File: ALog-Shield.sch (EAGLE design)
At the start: 26 parts, among them U1 DS3231MZ/V+T

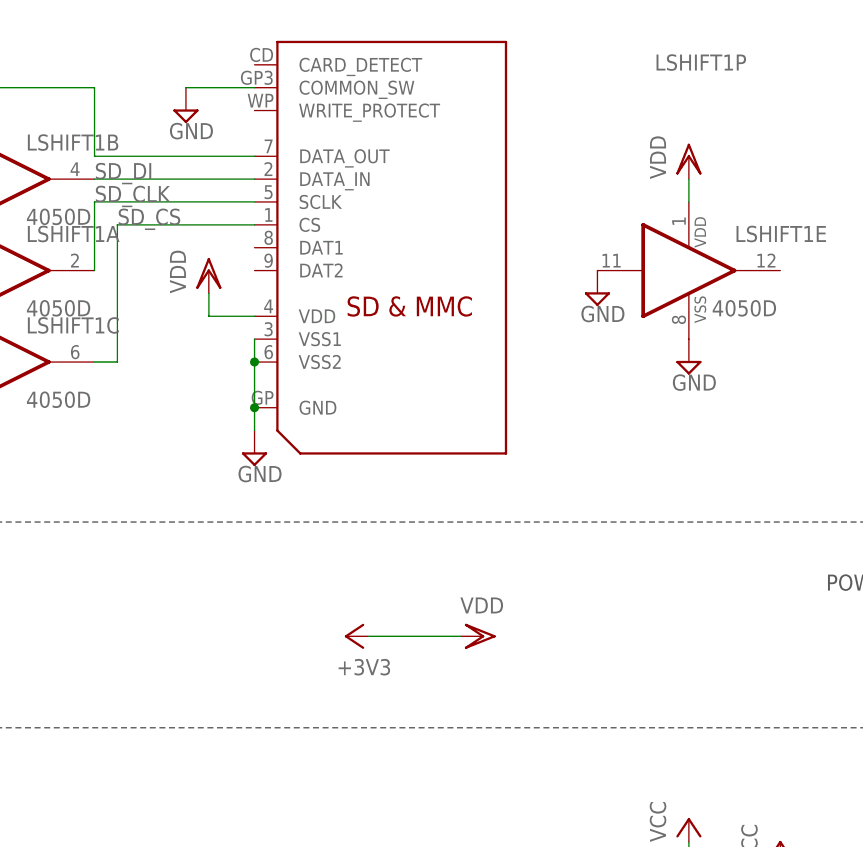
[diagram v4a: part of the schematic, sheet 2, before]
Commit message: 3V3 (not VDD) and VCC
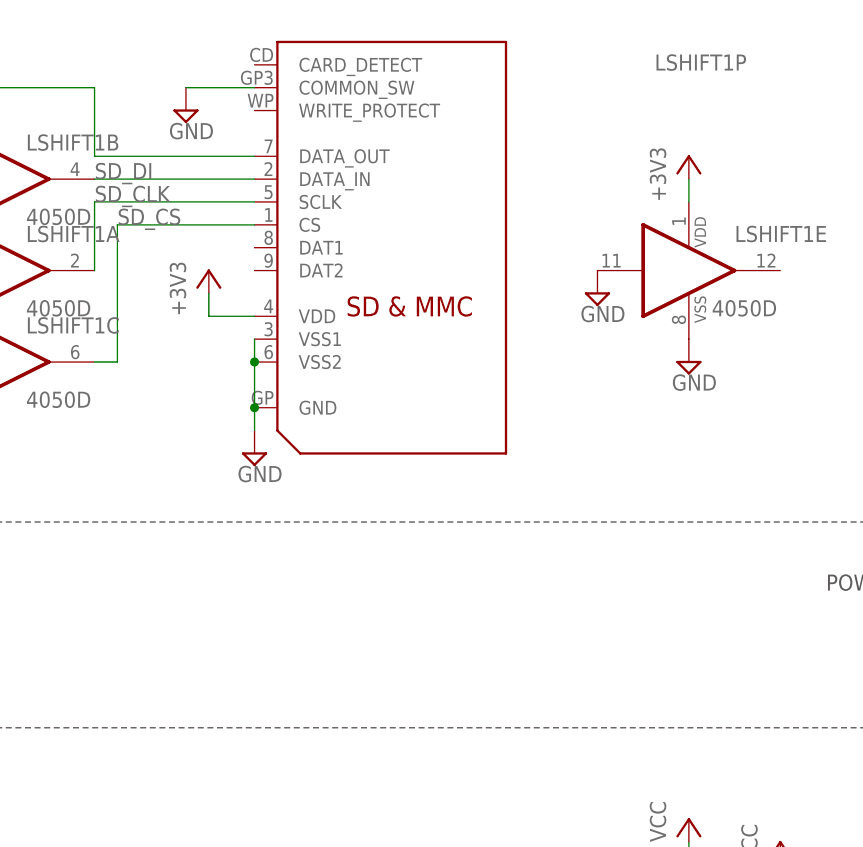
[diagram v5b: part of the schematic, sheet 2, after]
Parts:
- U$9: value ARDUINO_SHIELD_PIN_PURPOSE -> AWICKERT_ARDUINO_SHIELD_PIN_PURPOSE; device awickert:ARDUINO_SHIELD_PIN_PURPOSE -> ALog-Shield:AWICKERT_ARDUINO_SHIELD_PIN_PURPOSE
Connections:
- removed net VDD: LSHIFT1P.VDD, SD1.VDD
- new net VIN: U$9.VIN
- net +3V3: now also LSHIFT1P.VDD, SD1.VDD
- net VCC: now also U$9.5V; no longer U$9.VCC, U$9.VIN
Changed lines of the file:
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@@
 <?xml version="1.0" encoding="utf-8"?>
 <!DOCTYPE eagle SYSTEM "eagle.dtd">
-<eagle version="8.3.1">
+<eagle version="8.5.0">
 <drawing>
 <settings>
-<setting alwaysvectorfont="yes"/>
+<setting alwaysvectorfont="no"/>
 <setting keepoldvectorfont="yes"/>
 <setting verticaltext="up"/>
@@
 <layer number="59" name="tCarbon" color="7" fill="1" visible="no" active="no"/>
 <layer number="60" name="bCarbon" color="7" fill="1" visible="no" active="no"/>
+<layer number="88" name="SimResults" color="9" fill="1" visible="yes" active="yes"/>
+<layer number="89" name="SimProbes" color="9" fill="1" visible="yes" active="yes"/>
 <layer number="90" name="Modules" color="7" fill="1" visible="no" active="yes"/>
 <layer number="91" name="Nets" color="2" fill="1" visible="yes" active="yes"/>
@@
 </classes>
 <parts>
-<part name="U$9" library="awickert" deviceset="ARDUINO_SHIELD_PIN_PURPOSE" device=""/>
+<part name="U$9" library="ALog-Shield" deviceset="AWICKERT_ARDUINO_SHIELD_PIN_PURPOSE" device=""/>
 <part name="+3V3" library="supply1" deviceset="+3V3" device=""/>
 <part name="SUPPLY38" library="supply2" deviceset="GND" device=""/>
 <part name="SUPPLY39" library="supply2" deviceset="GND" device=""/>
 <part name="P+8" library="supply1" deviceset="VCC" device=""/>
-<part name="P+6" library="supply1" deviceset="VCC" device=""/>
 <part name="SUPPLY40" library="supply2" deviceset="GND" device=""/>
 <part name="+3V5" library="supply1" deviceset="+3V3" device=""/>
@@
 <part name="FRAME1" library="frames" deviceset="LETTER_P" device=""/>
 <part name="FRAME3" library="frames" deviceset="LETTER_P" device=""/>
-<part name="+3V15" library="supply1" deviceset="+3V3" device=""/>
-<part name="SD_3V4" library="supply1" deviceset="VDD" device=""/>
-<part name="SD_3V5" library="supply1" deviceset="VDD" device=""/>
-<part name="SD_3V6" library="supply1" deviceset="VDD" device=""/>
 <part name="+3V16" library="supply1" deviceset="+3V3" device=""/>
 <part name="+3V4" library="supply1" deviceset="+3V3" device=""/>
@@
 <part name="LOGO1" library="SparkFun-Aesthetics" deviceset="OSHW-LOGO" device="L"/>
 <part name="J3" library="SparkFun-Connectors" deviceset="M02" device="3.5MM"/>
+<part name="+3V2" library="supply1" deviceset="+3V3" device=""/>
+<part name="+3V7" library="supply1" deviceset="+3V3" device=""/>
 </parts>
 <sheets>
@@
 <instance part="SUPPLY39" gate="GND" x="160.02" y="-60.96"/>
 <instance part="P+8" gate="VCC" x="167.64" y="-53.34"/>
-<instance part="P+6" gate="VCC" x="142.24" y="-45.72"/>
 <instance part="SUPPLY40" gate="GND" x="134.62" y="-71.12"/>
 <instance part="+3V5" gate="G$1" x="152.4" y="-60.96"/>
@@
 <segment>
 <wire x1="124.46" y1="-58.42" x2="154.94" y2="-58.42" width="0.1524" layer="91"/>
-<pinref part="U$9" gate="G$1" pin="VCC"/>
+<pinref part="U$9" gate="G$1" pin="5V"/>
 <label x="129.54" y="-58.42" size="1.778" layer="95"/>
 <wire x1="154.94" y1="-58.42" x2="154.94" y2="-66.04" width="0.1524" layer="91"/>
@@
 <wire x1="154.94" y1="-71.12" x2="154.94" y2="-66.04" width="0.1524" layer="91"/>
 <junction x="154.94" y="-66.04"/>
-</segment>
-<segment>
-<wire x1="124.46" y1="-50.8" x2="142.24" y2="-50.8" width="0.1524" layer="91"/>
-<pinref part="U$9" gate="G$1" pin="VIN"/>
-<wire x1="142.24" y1="-50.8" x2="142.24" y2="-48.26" width="0.1524" layer="91"/>
-<pinref part="P+6" gate="VCC" pin="VCC"/>
 </segment>
 <segment>
@@
 <wire x1="137.16" y1="-139.7" x2="132.08" y2="-139.7" width="0.1524" layer="91"/>
 <label x="132.08" y="-139.7" size="1.778" layer="95"/>
+</segment>
+</net>
+<net name="VIN" class="0">
+<segment>
+<wire x1="124.46" y1="-50.8" x2="134.62" y2="-50.8" width="0.1524" layer="91"/>
+<pinref part="U$9" gate="G$1" pin="VIN"/>
+<label x="129.54" y="-50.8" size="1.778" layer="95"/>
 </segment>
 </net>
@@
 <attribute name="DRAWING_NAME" x="101.6" y="19.05" size="2.54" layer="94"/>
 </instance>
-<instance part="+3V15" gate="G$1" x="76.2" y="175.26" rot="R90"/>
-<instance part="SD_3V4" gate="G$1" x="91.44" y="175.26" rot="R270"/>
-<instance part="SD_3V5" gate="G$1" x="60.96" y="215.9"/>
-<instance part="SD_3V6" gate="G$1" x="114.3" y="228.6"/>
 <instance part="P+5" gate="VCC" x="124.46" y="152.4"/>
 <instance part="P+7" gate="VCC" x="114.3" y="154.94"/>
@@
 </instance>
 <instance part="CLOCK_BATT" gate="G$1" x="137.16" y="121.92" rot="R90"/>
+<instance part="+3V2" gate="G$1" x="60.96" y="215.9"/>
+<instance part="+3V7" gate="G$1" x="114.3" y="228.6"/>
 </instances>
 <busses>
@@
 </segment>
 </net>
-<net name="+3V3" class="0">
-<segment>
-<pinref part="SD_3V4" gate="G$1" pin="VDD"/>
-<pinref part="+3V15" gate="G$1" pin="+3V3"/>
-<wire x1="88.9" y1="175.26" x2="78.74" y2="175.26" width="0.1524" layer="91"/>
-</segment>
-</net>
 <net name="SCL" class="0">
 <segment>
@@
 </segment>
 </net>
-<net name="VDD" class="0">
-<segment>
-<wire x1="60.96" y1="210.82" x2="66.04" y2="210.82" width="0.1524" layer="91"/>
-<pinref part="SD1" gate="G$1" pin="VDD"/>
-<pinref part="SD_3V5" gate="G$1" pin="VDD"/>
-<wire x1="60.96" y1="210.82" x2="60.96" y2="213.36" width="0.1524" layer="91"/>
-</segment>
-<segment>
-<pinref part="LSHIFT1" gate="P" pin="VDD"/>
-<wire x1="114.3" y1="223.52" x2="114.3" y2="226.06" width="0.1524" layer="91"/>
-<pinref part="SD_3V6" gate="G$1" pin="VDD"/>
-</segment>
-</net>
 <net name="CS-SD" class="0">
 <segment>
@@
 </segment>
 </net>
+<net name="+3V3" class="0">
+<segment>
+<pinref part="LSHIFT1" gate="P" pin="VDD"/>
+<wire x1="114.3" y1="223.52" x2="114.3" y2="226.06" width="0.1524" layer="91"/>
+<pinref part="+3V7" gate="G$1" pin="+3V3"/>
+</segment>
+<segment>
+<wire x1="60.96" y1="210.82" x2="66.04" y2="210.82" width="0.1524" layer="91"/>
+<pinref part="SD1" gate="G$1" pin="VDD"/>
+<wire x1="60.96" y1="210.82" x2="60.96" y2="213.36" width="0.1524" layer="91"/>
+<pinref part="+3V2" gate="G$1" pin="+3V3"/>
+</segment>
+</net>

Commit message: Beta for review
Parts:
- added U$1: NWLOGO_MED, awickert:NWLOGO_MED
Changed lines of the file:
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@@
 <?xml version="1.0" encoding="utf-8"?>
 <!DOCTYPE eagle SYSTEM "eagle.dtd">
-<eagle version="8.5.0">
+<eagle version="8.3.1">
 <drawing>
 <settings>
@@
 <part name="+3V2" library="supply1" deviceset="+3V3" device=""/>
 <part name="+3V7" library="supply1" deviceset="+3V3" device=""/>
+<part name="U$1" library="awickert" deviceset="NWLOGO_MED" device=""/>
 </parts>
 <sheets>
@@
 <instance part="LOGO1" gate="G$1" x="17.78" y="-12.7"/>
 <instance part="J3" gate="G$1" x="144.78" y="-137.16" rot="R180"/>
+<instance part="U$1" gate="G$1" x="17.78" y="-27.94"/>
 </instances>
 <busses>

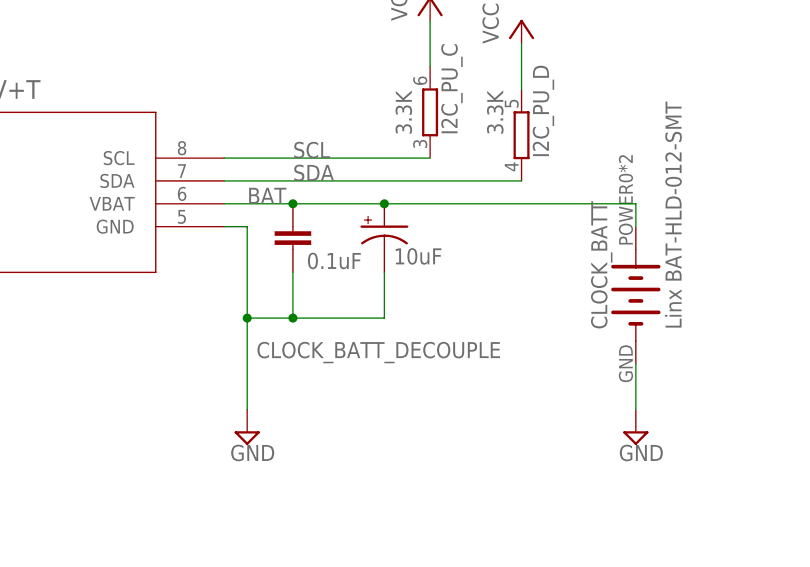
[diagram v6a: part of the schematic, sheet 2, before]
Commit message: 1206-->0805 10uF, rm floating vias
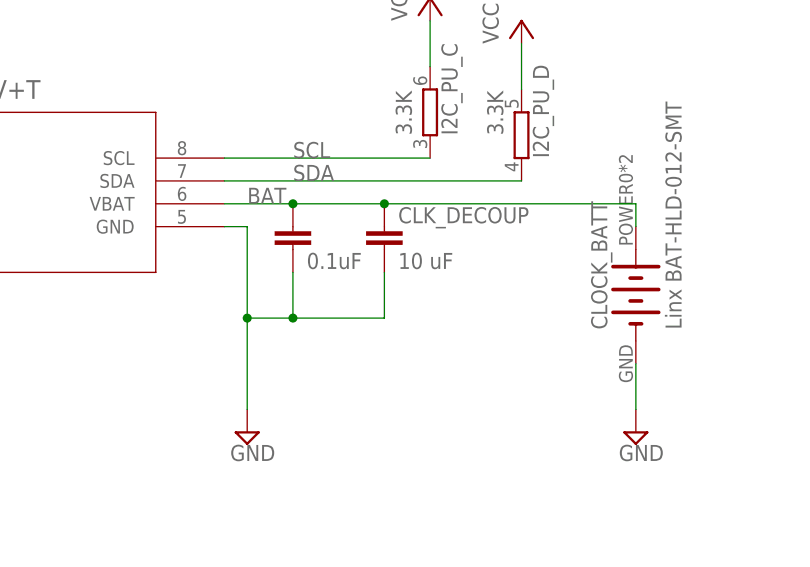
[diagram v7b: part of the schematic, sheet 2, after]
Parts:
- removed CLOCK_BATT_DECOUPLE: 10uF, SparkFun-Passives:CAP_POL1206
- added CLK_DECOUP: 10 uF, SparkFun-Passives:CAP0805
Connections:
- net BAT: now also CLK_DECOUP.1; no longer CLOCK_BATT_DECOUPLE.+
- net GND: now also CLK_DECOUP.2; no longer CLOCK_BATT_DECOUPLE.-
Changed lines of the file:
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@@
 <part name="D2" library="semicon-smd-ipc" deviceset="DIODE_AC-CA_" device="" value="BAT54"/>
 <part name="LOG" library="SparkFun-Electromechanical" deviceset="SWITCH-MOMENTARY-2" device="PTH" value="LOG"/>
-<part name="CLOCK_BATT_DECOUPLE" library="SparkFun-Passives" deviceset="CAP_POL" device="1206" value="10uF"/>
 <part name="U1" library="Maxim-DS3231MZ_8-SOIC" deviceset="DS3231MZ/V+T" device=""/>
 <part name="FRAME1" library="frames" deviceset="LETTER_P" device=""/>
@@
 <part name="+3V7" library="supply1" deviceset="+3V3" device=""/>
 <part name="U$1" library="awickert" deviceset="NWLOGO_MED" device=""/>
+<part name="CLK_DECOUP" library="SparkFun-Passives" deviceset="CAP" device="0805" value="10 uF"/>
 </parts>
 <sheets>
@@
 </segment>
 <segment>
-<wire x1="78.74" y1="-160.02" x2="104.14" y2="-160.02" width="0.1524" layer="91"/>
+<wire x1="58.42" y1="-160.02" x2="104.14" y2="-160.02" width="0.1524" layer="91"/>
 <label x="78.74" y="-160.02" size="1.778" layer="95"/>
 <pinref part="D2" gate="G$1" pin="A2"/>
@@
 </instance>
 <instance part="SUPPLY56" gate="GND" x="137.16" y="106.68"/>
-<instance part="CLOCK_BATT_DECOUPLE" gate="G$1" x="109.22" y="129.54" smashed="yes">
-<attribute name="NAME" x="94.996" y="114.935" size="1.778" layer="95"/>
-<attribute name="VALUE" x="110.236" y="125.349" size="1.778" layer="96"/>
-</instance>
 <instance part="U1" gate="A" x="20.32" y="137.16"/>
 <instance part="FRAME3" gate="G$1" x="0" y="0"/>
@@
 <instance part="+3V2" gate="G$1" x="60.96" y="215.9"/>
 <instance part="+3V7" gate="G$1" x="114.3" y="228.6"/>
+<instance part="CLK_DECOUP" gate="G$1" x="109.22" y="127"/>
 </instances>
 <busses>
@@
 <segment>
 <pinref part="CLOCK_BATT_DECOUP" gate="G$1" pin="2"/>
-<pinref part="CLOCK_BATT_DECOUPLE" gate="G$1" pin="-"/>
 <wire x1="99.06" y1="119.38" x2="99.06" y2="124.46" width="0.1524" layer="91"/>
 <wire x1="109.22" y1="124.46" x2="109.22" y2="119.38" width="0.1524" layer="91"/>
@@
 <junction x="99.06" y="119.38"/>
 <pinref part="U1" gate="A" pin="GND"/>
+<pinref part="CLK_DECOUP" gate="G$1" pin="2"/>
 </segment>
 <segment>
@@
 <label x="93.98" y="132.08" size="1.778" layer="95"/>
 <pinref part="CLOCK_BATT_DECOUP" gate="G$1" pin="1"/>
+<junction x="99.06" y="132.08"/>
 <wire x1="99.06" y1="132.08" x2="109.22" y2="132.08" width="0.1524" layer="91"/>
-<junction x="99.06" y="132.08"/>
-<pinref part="CLOCK_BATT_DECOUPLE" gate="G$1" pin="+"/>
+<pinref part="U1" gate="A" pin="VBAT"/>
 <wire x1="109.22" y1="132.08" x2="137.16" y2="132.08" width="0.1524" layer="91"/>
-<junction x="109.22" y="132.08"/>
-<pinref part="U1" gate="A" pin="VBAT"/>
 <wire x1="137.16" y1="132.08" x2="137.16" y2="129.54" width="0.1524" layer="91"/>
 <pinref part="CLOCK_BATT" gate="G$1" pin="+"/>
-</segment>
-</net>
+<pinref part="CLK_DECOUP" gate="G$1" pin="1"/>
+<junction x="109.22" y="132.08"/>
+</segment>
+</net>

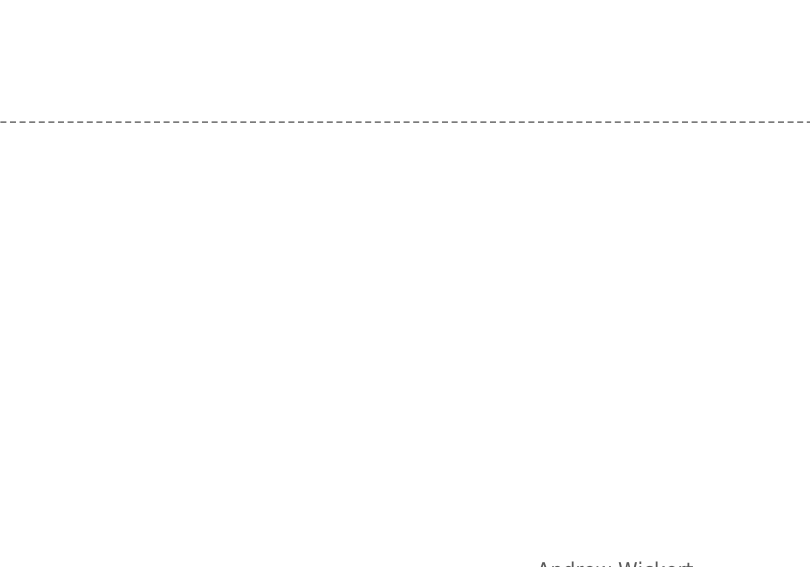
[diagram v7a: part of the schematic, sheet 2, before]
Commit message: AREF to 3V3 jumper
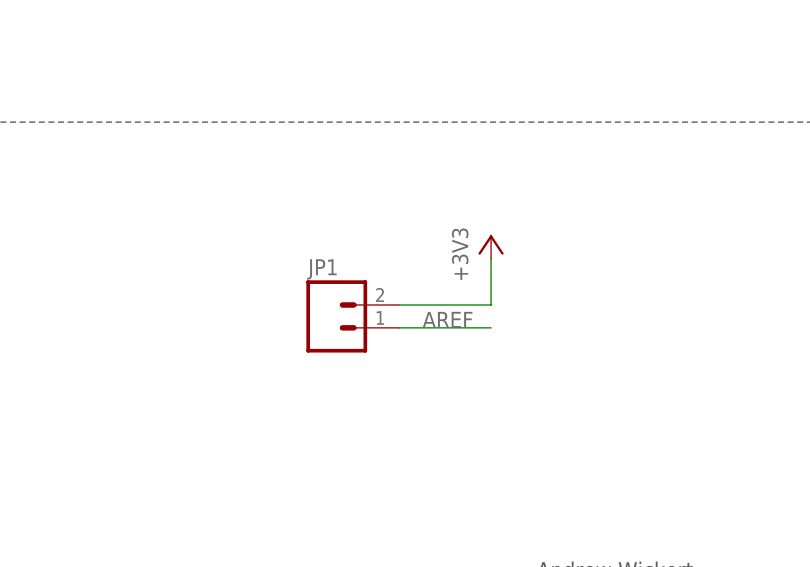
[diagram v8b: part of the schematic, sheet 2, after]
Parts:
- added JP1: (no value), SparkFun-Connectors:M02LOCK
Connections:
- new net AREF: JP1.1, U$9.AREF
- net +3V3: now also JP1.2; no longer U$9.AREF
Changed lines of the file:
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@@
 <parts>
 <part name="U$9" library="ALog-Shield" deviceset="AWICKERT_ARDUINO_SHIELD_PIN_PURPOSE" device=""/>
-<part name="+3V3" library="supply1" deviceset="+3V3" device=""/>
 <part name="SUPPLY38" library="supply2" deviceset="GND" device=""/>
 <part name="SUPPLY39" library="supply2" deviceset="GND" device=""/>
@@
 <part name="U$1" library="awickert" deviceset="NWLOGO_MED" device=""/>
 <part name="CLK_DECOUP" library="SparkFun-Passives" deviceset="CAP" device="0805" value="10 uF"/>
+<part name="JP1" library="SparkFun-Connectors" deviceset="M02" device="LOCK"/>
+<part name="+3V3" library="supply1" deviceset="+3V3" device=""/>
 </parts>
 <sheets>
@@
 <instances>
 <instance part="U$9" gate="G$1" x="91.44" y="-45.72" rot="R90"/>
-<instance part="+3V3" gate="G$1" x="43.18" y="-76.2" rot="R90"/>
 <instance part="SUPPLY38" gate="GND" x="35.56" y="-76.2"/>
 <instance part="SUPPLY39" gate="GND" x="160.02" y="-60.96"/>
@@
 <net name="+3V3" class="0">
 <segment>
-<wire x1="45.72" y1="-76.2" x2="63.5" y2="-76.2" width="0.1524" layer="91"/>
-<pinref part="U$9" gate="G$1" pin="AREF"/>
-<pinref part="+3V3" gate="G$1" pin="+3V3"/>
-</segment>
-<segment>
 <wire x1="124.46" y1="-60.96" x2="139.7" y2="-60.96" width="0.1524" layer="91"/>
 <pinref part="U$9" gate="G$1" pin="3V3_SWITCHED"/>
@@
 <pinref part="U$9" gate="G$1" pin="VIN"/>
 <label x="129.54" y="-50.8" size="1.778" layer="95"/>
+</segment>
+</net>
+<net name="AREF" class="0">
+<segment>
+<wire x1="53.34" y1="-76.2" x2="63.5" y2="-76.2" width="0.1524" layer="91"/>
+<pinref part="U$9" gate="G$1" pin="AREF"/>
+<label x="53.34" y="-76.2" size="1.778" layer="95"/>
 </segment>
 </net>
@@
 <instance part="+3V7" gate="G$1" x="114.3" y="228.6"/>
 <instance part="CLK_DECOUP" gate="G$1" x="109.22" y="127"/>
+<instance part="JP1" gate="G$1" x="129.54" y="58.42"/>
+<instance part="+3V3" gate="G$1" x="147.32" y="68.58"/>
 </instances>
 <busses>
@@
 <pinref part="+3V2" gate="G$1" pin="+3V3"/>
 </segment>
-</net>
+<segment>
+<pinref part="JP1" gate="G$1" pin="2"/>
+<pinref part="+3V3" gate="G$1" pin="+3V3"/>
+<wire x1="137.16" y1="60.96" x2="147.32" y2="60.96" width="0.1524" layer="91"/>
+<wire x1="147.32" y1="60.96" x2="147.32" y2="66.04" width="0.1524" layer="91"/>
+</segment>
+</net>
+<net name="AREF" class="0">
+<segment>
+<pinref part="JP1" gate="G$1" pin="1"/>
+<wire x1="137.16" y1="58.42" x2="147.32" y2="58.42" width="0.1524" layer="91"/>
+<label x="139.7" y="58.42" size="1.778" layer="95"/>
+</segment>
+</net>
